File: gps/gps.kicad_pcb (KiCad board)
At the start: 2 copper layers, 167 x 82.5 mm, 66 parts, among them J1 Conn_01x04, J10 Conn_01x02, J11 Conn_01x02, J2 Conn_01x04, J3 Conn_01x04, J4 Conn_01x04, J5 Conn_01x04, J6 Conn_01x04, J7 USB_B_Micro, J8 Conn_01x04, SW1 RotaryEncoder_Switch, U1 NEO-M8N, U10 M24C01-FMN, U2 TPS613226ADBV, U3 DFR0654, U4 HT16k33, U5 7seg_1x1_rgb, U6 7seg_1x1_rgb, U7 7seg_1x1_rgb, U8 CA56-12CGKWA, U9 DS3231M

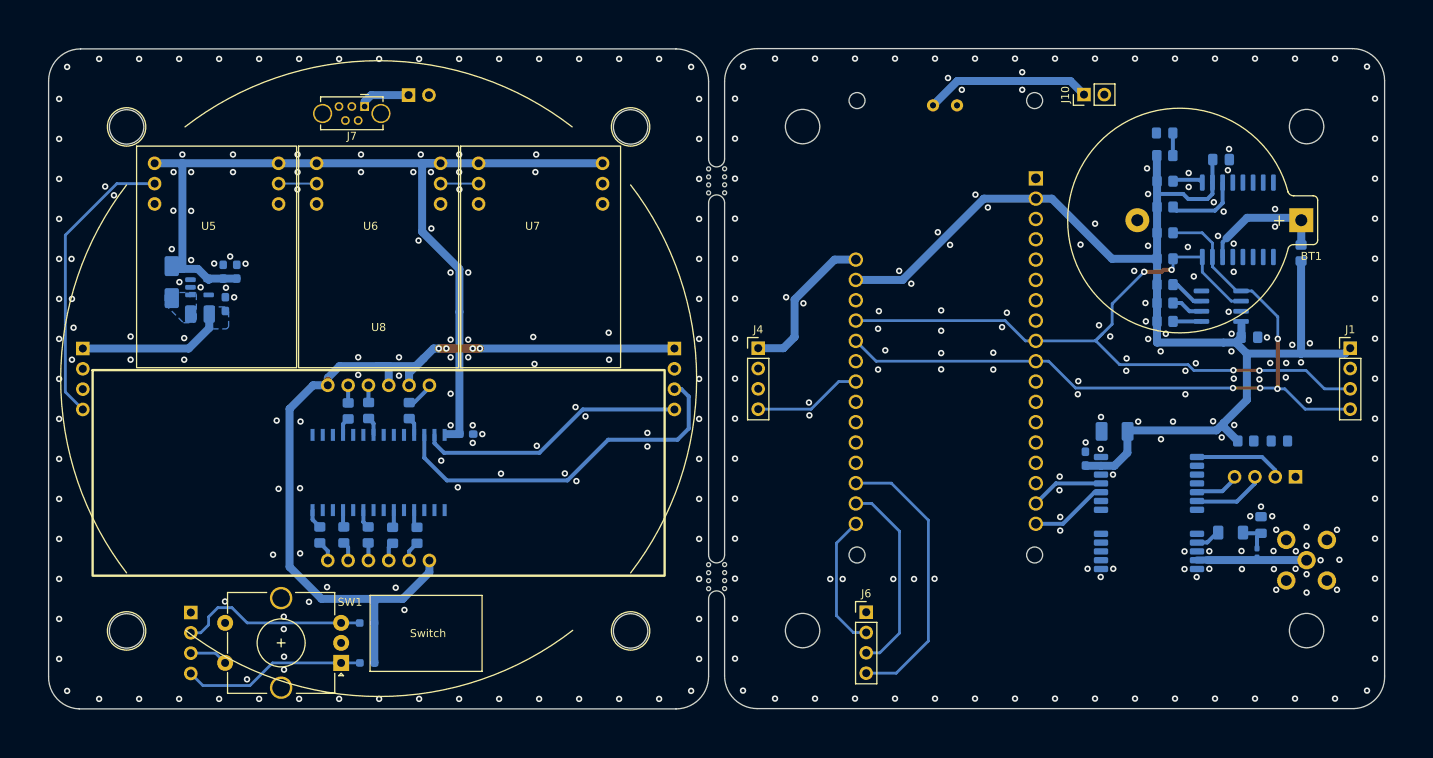
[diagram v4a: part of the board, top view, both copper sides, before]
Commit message: update pcb/housing
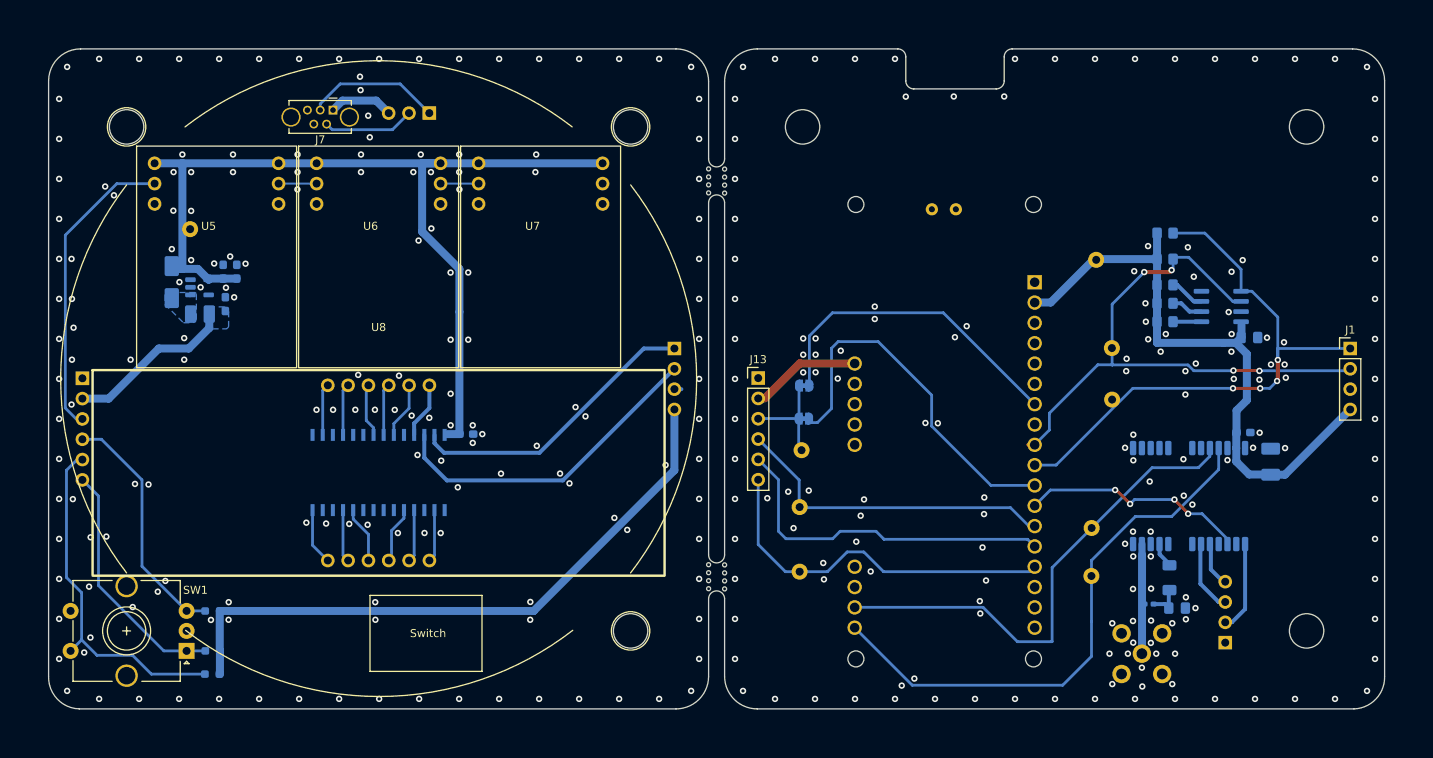
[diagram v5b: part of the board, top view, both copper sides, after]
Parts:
- removed BT1: Battery, Battery:BatteryHolder_Keystone_107_1x23mm
- removed C9: 100nF, Capacitor_SMD:C_0805_2012Metric_Pad1.18x1.45mm_HandSolder
- removed D1: LED_GR, LED_SMD:LED_0805_2012Metric_Pad1.15x1.40mm_HandSolder
- removed D3: LED, LED_SMD:LED_0805_2012Metric_Pad1.15x1.40mm_HandSolder
- removed J10: Conn_01x02, Connector_PinHeader_2.54mm:PinHeader_1x02_P2.54mm_Vertical
- removed J11: Conn_01x02, Connector_PinSocket_2.54mm:PinSocket_1x02_P2.54mm_Vertical
- removed J4, J6: Conn_01x04, Connector_PinHeader_2.54mm:PinHeader_1x04_P2.54mm_Vertical
- removed J5, J8: Conn_01x04, Connector_PinSocket_2.54mm:PinSocket_1x04_P2.54mm_Vertical
- removed R1: 1k5, Resistor_SMD:R_0805_2012Metric_Pad1.20x1.40mm_HandSolder
- removed R10, R3, R4, R5, R6, R7, R8, R9: 150, Resistor_SMD:R_0805_2012Metric_Pad1.20x1.40mm_HandSolder
- removed R13, R14: 4k7, Resistor_SMD:R_0805_2012Metric_Pad1.20x1.40mm_HandSolder
- removed R15: 200, Resistor_SMD:R_0805_2012Metric_Pad1.20x1.40mm_HandSolder
- removed R16: 1k, Resistor_SMD:R_0805_2012Metric_Pad1.20x1.40mm_HandSolder
- removed the REF** at (62.5, 114.5)
- removed the REF** at (147.0, 114.5)
- removed U9: DS3231M, Package_SO:SOIC-16W_7.5x10.3mm_P1.27mm
- added J12: ENC+RGB, Connector_PinSocket_2.54mm:PinSocket_1x06_P2.54mm_Vertical, B.Cu at (57.0, 82.9)
- added J13: ENC+RGB, Connector_PinHeader_2.54mm:PinHeader_1x06_P2.54mm_Vertical, F.Cu at (141.4, 82.9)
- added J9: USB_pads, Connector_PinSocket_2.54mm:PinSocket_1x03_P2.54mm_Vertical, B.Cu at (100.3, 49.8)
- added R_E3: 10k, Resistor_SMD:R_0603_1608Metric_Pad0.98x0.95mm_HandSolder, B.Cu at (73.2, 119.9)
- added TP1: SDA, TestPoint:TestPoint_Loop_D1.80mm_Drill1.0mm_Beaded, B.Cu at (185.7, 85.6)
- added TP10: Jumper_MOSI, Jumper:SolderJumper-2_P1.3mm_Bridged_RoundedPad1.0x1.5mm, B.Cu at (147.2, 83.8)
- added TP11: Jumper_D9, Jumper:SolderJumper-2_P1.3mm_Bridged_RoundedPad1.0x1.5mm, B.Cu at (147.2, 88.0)
- added TP2: SCL, TestPoint:TestPoint_Loop_D1.80mm_Drill1.0mm_Beaded, B.Cu at (185.7, 79.1)
- added TP3: RGB_7seg, TestPoint:TestPoint_Loop_D1.80mm_Drill1.0mm_Beaded, B.Cu at (146.9, 91.9)
- added TP4: GNSS_TXD, TestPoint:TestPoint_Loop_D1.80mm_Drill1.0mm_Beaded, B.Cu at (183.1, 101.6)
- added TP5: GNSS_RXD, TestPoint:TestPoint_Loop_D1.80mm_Drill1.0mm_Beaded, B.Cu at (183.1, 107.6)
- added TP6: +5V, TestPoint:TestPoint_Loop_D1.80mm_Drill1.0mm_Beaded, B.Cu at (70.4, 64.3)
- added TP7: +3V3, TestPoint:TestPoint_Loop_D1.80mm_Drill1.0mm_Beaded, B.Cu at (183.7, 68.1)
- added TP8: DT, TestPoint:TestPoint_Loop_D1.80mm_Drill1.0mm_Beaded, B.Cu at (146.6, 99.0)
- added TP9: CLK, TestPoint:TestPoint_Loop_D1.80mm_Drill1.0mm_Beaded, B.Cu at (146.6, 107.1)
- J1, J2: value Conn_01x04 -> I2C
- J3: value Conn_01x04 -> USB_pads
- U1: value NEO-M8N -> NEO-M9N
- U10: value M24C01-FMN -> 24C32
- U2: value TPS613226ADBV -> TPS613226ADBVR
- U3: footprint DFR0654:MODULE_DFR0654 -> DFR0654:DFR0654_2
- moved AE1 23.7 mm to (189.4, 117.3), turned to 0 degrees
- moved J3 22.5 mm to (199.8, 116.0), turned to 0 degrees
- moved C2 20.0 mm to (202.1, 89.7), turned to 0 degrees
- moved C1 19.9 mm to (205.5, 93.3), turned to 90 degrees
- moved R_E1 19.4 mm to (73.2, 112.0)
- moved R_E2 19.4 mm to (73.3, 117.0)
- moved SW1 19.4 mm to (70.0, 117.0)
- moved L1 14.9 mm to (190.3, 111.1), turned to 0 degrees
- moved C3 14.8 mm to (193.8, 111.6), turned to 180 degrees
- moved U3 12.5 mm to (166.2, 89.1)
- moved R2 9.49 mm to (192.9, 107.8), turned to -90 degrees
- moved U1 5.44 mm to (195.3, 97.6), turned to 90 degrees
- moved J7 3.98 mm to (88.3, 49.4)
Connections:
- J1 pad 1: +3V3 -> SDA
- J1 pad 2: GND -> SCL
- J1 pad 3: SCL -> GND
- J1 pad 4: SDA -> +3V3
- J2 pad 1: +3V3 -> SDA
- J2 pad 2: GND -> SCL
- J2 pad 3: SCL -> GND
- J2 pad 4: SDA -> +3V3
- J7 pad 1: VUSB -> Net-(J7-VBUS)
- J7 pad 2: unconnected-(J7-D--Pad2) -> Net-(J7-D-)
- J7 pad 3: unconnected-(J7-D+-Pad3) -> Net-(J7-D+)
- U1 pad 3: unconnected-(U1-TIMEPULSE-Pad3) -> PULSE
- U3 pad 11: unconnected-(U3-D9-Pad11) -> Net-(U3-D9)
- U3 pad 12: unconnected-(U3-D7-Pad12) -> PULSE
- U3 pad 13: unconnected-(U3-D6-Pad13) -> DT
- U3 pad 14: unconnected-(U3-D5-Pad14) -> SW
- U3 pad 15: unconnected-(U3-D3-Pad15) -> CLK
- U3 pad 17: GNSS_RXD -> unconnected-(U3-TX-Pad17)
- U3 pad 18: GNSS_TXD -> unconnected-(U3-RX-Pad18)
- U3 pad 19: DT -> GNSS_RXD
- U3 pad 20: SW -> GNSS_TXD
- U3 pad 21: CLK -> unconnected-(U3-D12-Pad21)
- U3 pad 33: VUSB -> unconnected-(U3-VUSB-Pad33)
- U3 pad 7: unconnected-(U3-MOSI-Pad7) -> Net-(U3-MOSI)
- U4 pad 10: unconnected-(U4-ROW15/k13/INT-Pad10) -> /Display/DPX
- U4 pad 16: unconnected-(U4-ROW9/K7-Pad16) -> /Display/CA1
- U4 pad 2: unconnected-(U4-COM0/AD-Pad2) -> /Display/CA4
- U4 pad 22: unconnected-(U4-ROW3/K1-Pad22) -> /Display/CA2
- U4 pad 23: unconnected-(U4-ROW2/A0-Pad23) -> /Display/CA3
- U4 pad 5: unconnected-(U4-COM3/KS2-Pad5) -> /Display/c
- U4 pad 6: /Display/c -> unconnected-(U4-COM4-Pad6)
- U4 pad 9: /Display/DPX -> unconnected-(U4-COM7-Pad9)
- U8 pad 1: Net-(U8-e) -> /Display/e
- U8 pad 10: Net-(U8-f) -> /Display/f
- U8 pad 11: Net-(U8-a) -> /Display/a
- U8 pad 12: +3V3 -> /Display/CA1
- U8 pad 2: Net-(U8-d) -> /Display/d
- U8 pad 3: Net-(U8-DPX) -> /Display/DPX
- U8 pad 4: Net-(U8-c) -> /Display/c
- U8 pad 5: Net-(U8-g) -> /Display/g
- U8 pad 6: +3V3 -> /Display/CA4
- U8 pad 7: Net-(U8-b) -> /Display/b
- U8 pad 8: +3V3 -> /Display/CA3
- U8 pad 9: +3V3 -> /Display/CA2
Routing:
- net +3V3: track 264.7 -> 158.6 mm, vias 4 -> 0
- net GNSS_RXD: track 9.18 -> 69.4 mm
- net SW: track 29.6 -> 87.3 mm
- net GNSS_TXD: track 9.97 -> 62.2 mm
- net Net-(U3-D9): track 0.00 -> 46.5 mm
- net Net-(U3-MOSI): track 0.00 -> 40.3 mm
- net DT: track 40.9 -> 71.6 mm
- net PULSE: track 0.00 -> 28.8 mm, vias 0 -> 4
- net VUSB: track 27.3 -> 0.00 mm
- net SCL: track 141.5 -> 116.3 mm
- net CLK: track 58.5 -> 77.1 mm
- net SDA: track 127.3 -> 109.1 mm
- net Net-(J7-D+): track 0.00 -> 17.0 mm
- net +BATT: track 16.2 -> 0.00 mm
- net Net-(J7-D-): track 0.00 -> 11.4 mm
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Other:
- outline, holes or cut-outs redrawn
- board text added: "Cut pro kabely | V"
- board text removed: "<-- posunout nahoru"

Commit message: update
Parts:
- removed the REF** at (125.5, 114.5)
- added DS1: LTC-4724JF, Display_7Segment:LTC4724JF, F.Cu at (85.1, 119.9)
- added J4: BATT, 1769:1769, B.Cu at (129.8, 102.2)
- added J5: ESP, Connector_PinSocket_2.54mm:PinSocket_1x02_P2.54mm_Vertical, B.Cu at (127.2, 94.8)
- added R1: 0R, Resistor_SMD:R_0805_2012Metric_Pad1.20x1.40mm_HandSolder, B.Cu at (69.5, 59.9)
- added REF**: MountingHole_3.2mm_M3, MountingHole:MountingHole_3.2mm_M3, F.Cu at (125.5, 114.5)
- added SW2: SW_DPDT_x2, Button_Switch_THT:MSN22AFW01, F.Cu at (115.6, 115.7)
- added TP12: IO22, TestPoint:TestPoint_Loop_D1.80mm_Drill1.0mm_Beaded, B.Cu at (146.8, 112.2)
- added TP13: IO21, TestPoint:TestPoint_Loop_D1.80mm_Drill1.0mm_Beaded, B.Cu at (146.8, 116.8)
- C7: value 0.1uF -> 100nF; footprint Capacitor_SMD:C_0603_1608Metric_Pad1.08x0.95mm_HandSolder -> Capacitor_SMD:C_0805_2012Metric_Pad1.18x1.45mm_HandSolder
- J1: value I2C -> I2C_H
- J2: value I2C -> I2C_S
- REF** (x2): value MountingHole_4.3mm_M4 -> MountingHole_3.2mm_M3; footprint MountingHole:MountingHole_4.3mm_M4 -> MountingHole:MountingHole_3.2mm_M3
- R_E1, R_E2, R_E3: footprint Resistor_SMD:R_0603_1608Metric_Pad0.98x0.95mm_HandSolder -> Resistor_SMD:R_0805_2012Metric_Pad1.20x1.40mm_HandSolder
- TP10, TP11: footprint Jumper:SolderJumper-2_P1.3mm_Bridged_RoundedPad1.0x1.5mm -> Resistor_SMD:R_0805_2012Metric_Pad1.20x1.40mm_HandSolder
- U2: value TPS613226ADBVR -> TPS613222ADBVR
- U8: value CA56-12CGKWA -> KW4-804AGB
- moved J7 7.44 mm to (95.7, 48.6)
- moved J9 7.44 mm to (107.7, 49.0)
- moved U3 2.45 mm to (164.5, 90.8)
- moved TP10 1.26 mm to (147.2, 85.1)
- moved R_E2 0.06 mm to (73.2, 117.0)
- moved R_E3 0.06 mm to (73.2, 120.0)
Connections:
- C5 pad 1: +5V -> Net-(D2-K)
- C6 pad 1: +5V -> Net-(D2-K)
- D2 pad 1: +5V -> Net-(D2-K)
- TP11 pad 1: Net-(U3-D9) -> Net-(U3-D7)
- TP6 pad 1: +5V -> Net-(D2-K)
- U2 pad 4: +5V -> Net-(D2-K)
- U3 pad 11: Net-(U3-D9) -> unconnected-(U3-D9-Pad11)
- U3 pad 12: PULSE -> Net-(U3-D7)
- U3 pad 13: DT -> PULSE
- U3 pad 14: SW -> unconnected-(U3-D5-Pad14)
- U3 pad 15: CLK -> SW
- U3 pad 16: unconnected-(U3-D2-Pad16) -> CLK
- U3 pad 21: unconnected-(U3-D12-Pad21) -> Net-(U3-D12)
- U3 pad 22: unconnected-(U3-D13-Pad22) -> Net-(U3-D13)
- U4 pad 10: /Display/DPX -> unconnected-(U4-ROW15/k13/INT-Pad10)
- U4 pad 11: /Display/d -> /Display/aF
- U4 pad 12: unconnected-(U4-ROW13/K11-Pad12) -> /Display/aBL2
- U4 pad 13: unconnected-(U4-ROW12/K10-Pad13) -> /Display/aAL1
- U4 pad 14: /Display/e -> /Display/aDP
- U4 pad 15: unconnected-(U4-ROW10/K8-Pad15) -> /Display/aE
- U4 pad 17: unconnected-(U4-ROW8/K6-Pad17) -> /Display/aCL3
- U4 pad 18: /Display/a -> unconnected-(U4-ROW7/K5-Pad18)
- U4 pad 19: unconnected-(U4-ROW6/K4-Pad19) -> /Display/aD
- U4 pad 2: /Display/CA4 -> /Display/CC3
- U4 pad 21: /Display/f -> unconnected-(U4-ROW4/K2-Pad21)
- U4 pad 24: unconnected-(U4-ROW1/A1-Pad24) -> /Display/CA4
- U4 pad 25: /Display/b -> /Display/aG
- U4 pad 3: unconnected-(U4-COM1/KS0-Pad3) -> /Display/f
- U4 pad 4: /Display/g -> /Display/b
- U4 pad 5: /Display/c -> /Display/g
- U4 pad 6: unconnected-(U4-COM4-Pad6) -> /Display/CC2
- U4 pad 7: unconnected-(U4-COM5-Pad7) -> /Display/CC1
- U4 pad 8: unconnected-(U4-COM6-Pad8) -> /Display/d
- U4 pad 9: unconnected-(U4-COM7-Pad9) -> /Display/L123
- U8 pad 1: /Display/e -> /Display/L123
- U8 pad 11: /Display/a -> /Display/CC3
- U8 pad 3: /Display/DPX -> /Display/CC1
- U8 pad 4: /Display/c -> /Display/CC2
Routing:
- net /Display/CC3: track 0.00 -> 62.3 mm
- net /Display/aE: track 0.00 -> 48.0 mm, vias 0 -> 2
- net /Display/b: track 6.99 -> 53.9 mm
- net Net-(U3-D9): track 46.5 -> 0.00 mm
- net /Display/aD: track 0.00 -> 46.4 mm, vias 0 -> 2
- net Net-(U3-D7): track 0.00 -> 46.2 mm
- net /Display/aCL3: track 0.00 -> 43.5 mm, vias 0 -> 2
- net /Display/aDP: track 0.00 -> 37.8 mm, vias 0 -> 2
- net /Display/f: track 6.69 -> 44.0 mm
- net /Display/CC1: track 0.00 -> 30.8 mm, vias 0 -> 1
- net Net-(J5-Pin_1): track 0.00 -> 30.0 mm
- net /Display/aG: track 0.00 -> 25.0 mm
- net /Display/CC2: track 0.00 -> 21.8 mm
- net +5V: track 118.9 -> 98.5 mm
- net DT: track 71.6 -> 52.3 mm
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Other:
- board text added: "+"
- board text added: "-"
- board text added: "BATT 9,5x55x65"
- board text removed: "Switch"

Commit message: PCB-update
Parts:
- J1: value I2C_H -> I2C/BATT_H; footprint Connector_PinHeader_2.54mm:PinHeader_1x04_P2.54mm_Vertical -> Connector_PinHeader_2.54mm:PinHeader_1x07_P2.54mm_Vertical
- J2: value I2C_S -> I2C/BATT_S; footprint Connector_PinSocket_2.54mm:PinSocket_1x04_P2.54mm_Vertical -> Connector_PinSocket_2.54mm:PinSocket_1x07_P2.54mm_Vertical
- SW1: footprint Rotary_Encoder:RotaryEncoder_Alps_EC12E-Switch_Vertical_H20mm_CircularMountingHoles -> Rotary_Encoder:RotaryEncoder_20mm_WO_mount_holes
- moved J4 92.3 mm to (214.5, 65.3)
- moved SW2 63.4 mm to (101.0, 53.9)
- moved J9 31.0 mm to (76.8, 49.5)
- moved J5 28.4 mm to (142.7, 71.0), turned to 0 degrees
- moved J3 22.0 mm to (202.7, 94.2), turned to 180 degrees
- moved C2 19.5 mm to (184.3, 97.7), turned to 90 degrees
- moved C1 17.6 mm to (188.0, 94.2), turned to 180 degrees
- moved TP5 12.3 mm to (180.9, 119.7)
- moved L1 11.7 mm to (202.0, 111.8)
- moved AE1 11.5 mm to (200.9, 117.9)
- moved TP4 11.5 mm to (180.6, 112.8)
- moved C3 10.2 mm to (203.9, 110.2)
- moved J7 9.86 mm to (85.8, 48.6)
- moved R2 9.60 mm to (202.5, 108.0), turned to 0 degrees
- moved SW1 7.91 mm to (62.5, 114.5)
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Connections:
- J1 pad 1: SDA -> SW_BATT
- J1 pad 2: SCL -> SW_ESP
- J1 pad 4: +3V3 -> SDA
- J2 pad 1: SDA -> SW_BATT
- J2 pad 2: SCL -> SW_ESP
- J2 pad 4: +3V3 -> SDA
- J4 pad 1: Net-(J4-Pin_1) -> SW_BATT
- J5 pad 1: Net-(J5-Pin_1) -> SW_ESP
- SW2 pad 1: Net-(J5-Pin_1) -> SW_ESP
- SW2 pad 2: Net-(J4-Pin_1) -> SW_BATT
- U1 pad 22: unconnected-(U1-V_BCKP-Pad22) -> +3V3
- U1 pad 5: Net-(J3-Pin_4) -> Net-(J3-Pin_3)
- U1 pad 6: Net-(J3-Pin_3) -> Net-(J3-Pin_4)
- U4 pad 12: /Display/aBL2 -> /Display/aAL1
- U4 pad 13: /Display/aAL1 -> /Display/aBL2
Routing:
- net SW_ESP: track 0.00 -> 147.2 mm
- net SW_BATT: track 0.00 -> 58.0 mm
- net Net-(J5-Pin_1): track 30.0 -> 0.00 mm
- net Net-(J4-Pin_1): track 18.3 -> 0.00 mm
- net GNSS_TXD: track 62.2 -> 44.0 mm
- net +3V3: track 168.9 -> 183.5 mm
- net GNSS_RXD: track 69.4 -> 55.1 mm
- net /Display/aBL2: track 18.1 -> 30.9 mm, vias 2 -> 0
- net Net-(J7-VBUS): track 8.10 -> 18.5 mm
- net /Display/aAL1: track 17.7 -> 25.3 mm, vias 2 -> 0
- net /Display/CC1: track 30.8 -> 23.8 mm
- net Net-(J3-Pin_2): track 11.3 -> 4.73 mm
- net Net-(J7-D+): track 17.0 -> 10.5 mm
- net Net-(AE1-A): track 13.7 -> 8.56 mm
- net Net-(J3-Pin_3): track 9.03 -> 5.51 mm
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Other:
- outline, holes or cut-outs redrawn

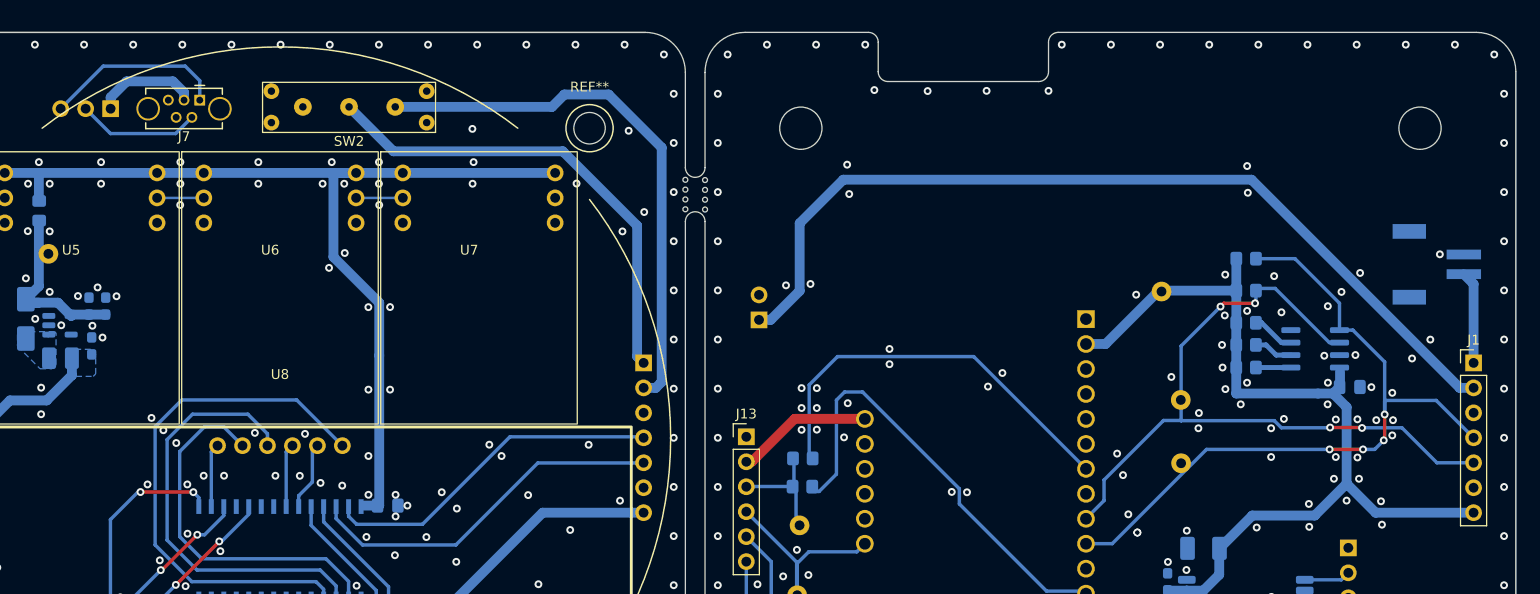
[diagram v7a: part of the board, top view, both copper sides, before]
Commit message: PCB-tweaked-BattConn
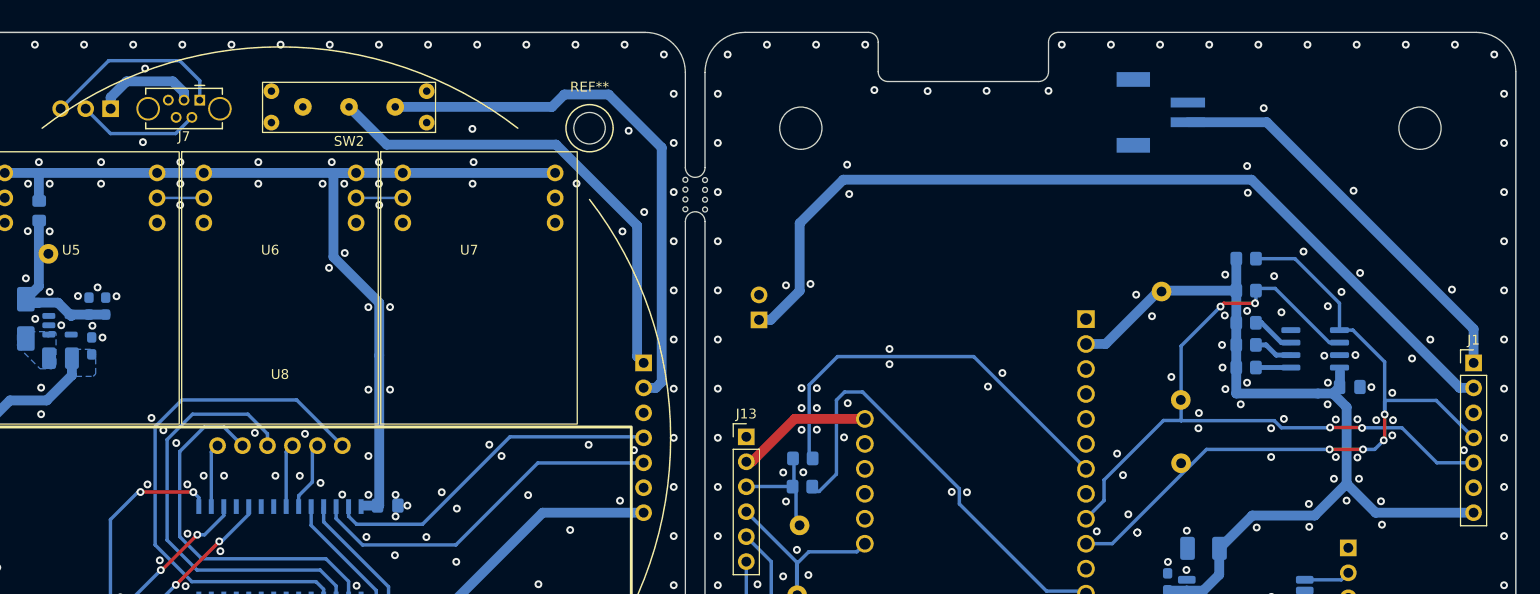
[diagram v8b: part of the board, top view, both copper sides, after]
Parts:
- moved J4 32.1 mm to (186.4, 49.9)
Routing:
- net SW_BATT: track 58.0 -> 89.8 mm
- net GND: vias 378 -> 390
